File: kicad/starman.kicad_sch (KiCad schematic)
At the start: 204 parts, among them J10 Barrel_Jack_MountingPin, J5 Conn_02x03_Counter_Clockwise, J7 Conn_01x10, J9 Conn_01x10, SW1 SW_SPST, SW2 SW_SPST, U1 ESP32-S2-MINI-1, U2 PCA9959, U3 PCA9959, U4 PCA9959, U5 PCA9959, U6 PCA9959, U7 PCA9959, U8 NCP59301, U9 LF33, Y1 20Mhz, Y2 20Mhz, Y3 20Mhz, Y4 20Mhz, Y5 20Mhz, Y6 20Mhz

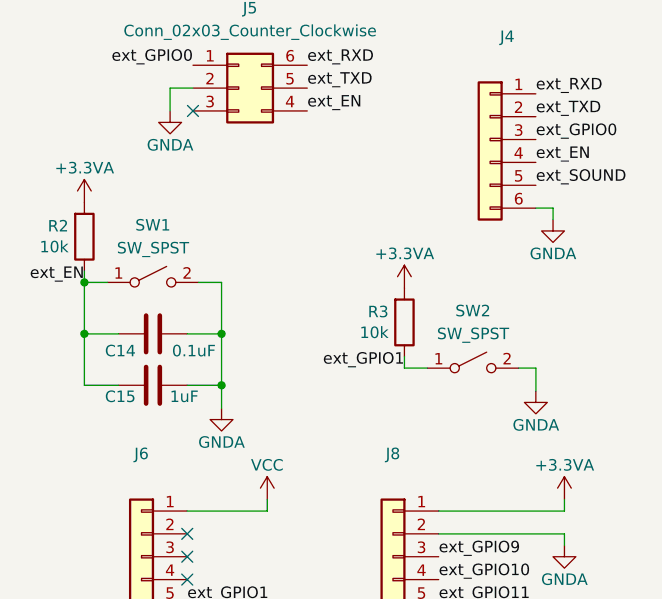
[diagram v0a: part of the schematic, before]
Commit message: Add on headers for an external "Play" button
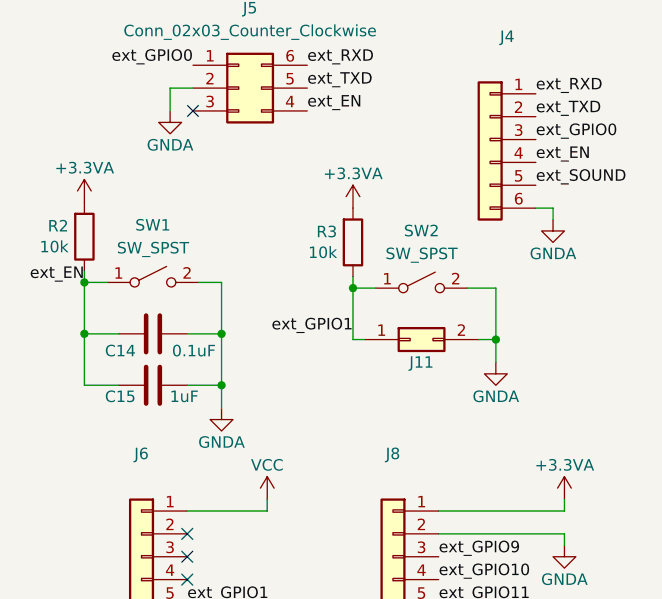
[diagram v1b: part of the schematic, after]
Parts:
- added J11: (no value), symbol Connector_Generic:Conn_02x01
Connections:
- net GNDA: now also J11.2 (Pin_2)
- net ext_GPIO1: now also J11.1 (Pin_1)
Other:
- moved on the sheet: R3, SW2
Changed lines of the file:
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@@
   (junction (at 210.82 88.9) (diameter 0) (color 0 0 0 0)
   )
+  (junction (at 398.145 55.88) (diameter 0) (color 0 0 0 0)
+  )
   (junction (at 144.78 143.51) (diameter 0) (color 0 0 0 0)
   )
@@
   (junction (at 78.74 153.67) (diameter 0) (color 0 0 0 0)
   )
+  (junction (at 382.27 50.165) (diameter 0) (color 0 0 0 0)
+  )
   (junction (at 144.78 45.72) (diameter 0) (color 0 0 0 0)
   )
@@
     (stroke (width 0) (type default) (color 0 0 0 0))
   )
+  (wire (pts (xy 398.145 55.88) (xy 398.145 50.165))
+    (stroke (width 0) (type default) (color 0 0 0 0))
+  )
   (wire (pts (xy 243.84 92.71) (xy 243.84 95.25))
     (stroke (width 0) (type default) (color 0 0 0 0))
@@
     (stroke (width 0) (type default) (color 0 0 0 0))
   )
-  (wire (pts (xy 400.685 59.055) (xy 402.59 59.055))
+  (wire (pts (xy 396.24 55.88) (xy 398.145 55.88))
     (stroke (width 0) (type default) (color 0 0 0 0))
   )
@@
     (stroke (width 0) (type default) (color 0 0 0 0))
   )
+  (wire (pts (xy 382.27 55.88) (xy 383.54 55.88))
+    (stroke (width 0) (type default) (color 0 0 0 0))
+  )
   (wire (pts (xy 144.78 81.28) (xy 142.24 81.28))
     (stroke (width 0) (type default) (color 0 0 0 0))
@@
     (stroke (width 0) (type default) (color 0 0 0 0))
   )
-  (wire (pts (xy 387.985 59.055) (xy 390.525 59.055))
+  (wire (pts (xy 382.27 50.165) (xy 384.81 50.165))
     (stroke (width 0) (type default) (color 0 0 0 0))
   )
@@
     (stroke (width 0) (type default) (color 0 0 0 0))
   )
+  (wire (pts (xy 382.27 50.165) (xy 382.27 55.88))
+    (stroke (width 0) (type default) (color 0 0 0 0))
+  )
   (wire (pts (xy 154.94 115.57) (xy 154.94 114.3))
     (stroke (width 0) (type default) (color 0 0 0 0))
@@
     (stroke (width 0) (type default) (color 0 0 0 0))
   )
+  (wire (pts (xy 398.145 50.165) (xy 394.97 50.165))
+    (stroke (width 0) (type default) (color 0 0 0 0))
+  )
   (wire (pts (xy 144.78 50.8) (xy 142.24 50.8))
     (stroke (width 0) (type default) (color 0 0 0 0))
@@
     (stroke (width 0) (type default) (color 0 0 0 0))
   )
-  (wire (pts (xy 387.985 57.785) (xy 387.985 59.055))
+  (wire (pts (xy 382.27 48.895) (xy 382.27 50.165))
     (stroke (width 0) (type default) (color 0 0 0 0))
   )
@@
     (stroke (width 0) (type default) (color 0 0 0 0))
   )
-  (wire (pts (xy 402.59 59.055) (xy 402.59 61.595))
+  (wire (pts (xy 398.145 55.88) (xy 398.145 58.42))
     (stroke (width 0) (type default) (color 0 0 0 0))
   )
@@
     (effects (font (size 1.27 1.27)) (justify right bottom))
   )
-  (label "ext_GPIO1" (at 387.985 59.055 180)
+  (label "ext_GPIO1" (at 382.27 55.245 180)
     (effects (font (size 1.27 1.27)) (justify right bottom))
   )
@@
     (pin "1")
   )
-  (symbol (lib_id "Device:R") (at 387.985 53.975 0) (mirror x) (unit 1)
+  (symbol (lib_id "Device:R") (at 382.27 45.085 0) (mirror x) (unit 1)
     (in_bom yes) (on_board yes)
-    (property "Reference" "R3" (id 0) (at 386.2324 52.8066 0)
+    (property "Reference" "R3" (id 0) (at 380.5174 43.9166 0)
       (effects (font (size 1.27 1.27)) (justify right))
     )
-    (property "Value" "10k" (id 1) (at 386.2324 55.118 0)
+    (property "Value" "10k" (id 1) (at 380.5174 46.228 0)
       (effects (font (size 1.27 1.27)) (justify right))
     )
-    (property "Footprint" "Resistor_SMD:R_0805_2012Metric" (id 2) (at 386.207 53.975 90)
+    (property "Footprint" "Resistor_SMD:R_0805_2012Metric" (id 2) (at 380.492 45.085 90)
       (effects (font (size 1.27 1.27)) hide)
     )
-    (property "Datasheet" "~" (id 3) (at 387.985 53.975 0)
+    (property "Datasheet" "~" (id 3) (at 382.27 45.085 0)
       (effects (font (size 1.27 1.27)) hide)
     )
@@
     (pin "1")
   )
-  (symbol (lib_id "power:GNDA") (at 402.59 61.595 0) (unit 1)
+  (symbol (lib_id "power:GNDA") (at 398.145 58.42 0) (unit 1)
     (in_bom yes) (on_board yes)
-    (property "Reference" "#PWR031" (id 0) (at 402.59 67.945 0)
+    (property "Reference" "#PWR031" (id 0) (at 398.145 64.77 0)
       (effects (font (size 1.27 1.27)) hide)
     )
-    (property "Value" "GNDA" (id 1) (at 402.59 65.405 0))
-    (property "Footprint" "" (id 2) (at 402.59 61.595 0)
+    (property "Value" "GNDA" (id 1) (at 398.145 62.23 0))
+    (property "Footprint" "" (id 2) (at 398.145 58.42 0)
       (effects (font (size 1.27 1.27)) hide)
     )
-    (property "Datasheet" "" (id 3) (at 402.59 61.595 0)
+    (property "Datasheet" "" (id 3) (at 398.145 58.42 0)
       (effects (font (size 1.27 1.27)) hide)
     )
     (pin "1")
   )
-  (symbol (lib_id "power:+3.3VA") (at 387.985 50.165 0) (unit 1)
+  (symbol (lib_id "Connector_Generic:Conn_02x01") (at 388.62 55.88 0) (unit 1)
     (in_bom yes) (on_board yes)
-    (property "Reference" "#PWR030" (id 0) (at 387.985 53.975 0)
+    (property "Reference" "J11" (id 0) (at 389.89 58.42 0))
+    (property "Value" "" (id 1) (at 389.89 60.96 0))
+    (property "Footprint" "" (id 2) (at 388.62 55.88 0)
       (effects (font (size 1.27 1.27)) hide)
     )
-    (property "Value" "+3.3VA" (id 1) (at 387.985 46.355 0))
-    (property "Footprint" "" (id 2) (at 387.985 50.165 0)
+    (property "Datasheet" "~" (id 3) (at 388.62 55.88 0)
       (effects (font (size 1.27 1.27)) hide)
     )
-    (property "Datasheet" "" (id 3) (at 387.985 50.165 0)
+    (pin "1")
+    (pin "2")
+  )
+  (symbol (lib_id "power:+3.3VA") (at 382.27 41.275 0) (unit 1)
+    (in_bom yes) (on_board yes)
+    (property "Reference" "#PWR030" (id 0) (at 382.27 45.085 0)
+      (effects (font (size 1.27 1.27)) hide)
+    )
+    (property "Value" "+3.3VA" (id 1) (at 382.27 37.465 0))
+    (property "Footprint" "" (id 2) (at 382.27 41.275 0)
+      (effects (font (size 1.27 1.27)) hide)
+    )
+    (property "Datasheet" "" (id 3) (at 382.27 41.275 0)
       (effects (font (size 1.27 1.27)) hide)
     )
@@
     (pin "1")
   )
-  (symbol (lib_id "Switch:SW_SPST") (at 395.605 59.055 0) (unit 1)
+  (symbol (lib_id "Switch:SW_SPST") (at 389.89 50.165 0) (unit 1)
     (in_bom yes) (on_board yes)
-    (property "Reference" "SW2" (id 0) (at 395.605 52.705 0))
-    (property "Value" "SW_SPST" (id 1) (at 395.605 55.245 0))
-    (property "Footprint" "Button_Switch_SMD:SW_SPST_PTS810" (id 2) (at 395.605 59.055 0)
+    (property "Reference" "SW2" (id 0) (at 389.89 43.815 0))
+    (property "Value" "SW_SPST" (id 1) (at 389.89 46.355 0))
+    (property "Footprint" "Button_Switch_SMD:SW_SPST_PTS810" (id 2) (at 389.89 50.165 0)
       (effects (font (size 1.27 1.27)) hide)
     )
-    (property "Datasheet" "~" (id 3) (at 395.605 59.055 0)
+    (property "Datasheet" "~" (id 3) (at 389.89 50.165 0)
       (effects (font (size 1.27 1.27)) hide)
     )
@@
       (reference "J10") (unit 1) (value "Barrel_Jack_MountingPin") (footprint "Connector_BarrelJack:BarrelJack_CUI_PJ-063AH_Horizontal")
     )
+    (path "/56bd17ef-9eb8-4409-8c35-c6c9960995e7"
+      (reference "J11") (unit 1) (value "Conn_02x01") (footprint "Connector_PinHeader_2.54mm:PinHeader_1x02_P2.54mm_Vertical")
+    )
     (path "/515a2d72-1a9d-4aa4-9d0c-cba89acc2e38"

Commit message: Fixed the solderpad for U2..U7 according to match datasheet
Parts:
- J1, J3: value (none) -> M20-8771246; footprint (none) -> Connector_PinHeader_2.54mm:PinHeader_1x12_P2.54mm_Vertical_SMD_Pin1Right
- J11: value (none) -> Conn_02x01; footprint (none) -> Connector_PinHeader_2.54mm:PinHeader_1x02_P2.54mm_Vertical
- J2: value (none) -> M20-8771246; footprint (none) -> Connector_PinHeader_2.54mm:PinHeader_1x06_P2.54mm_Vertical_SMD_Pin1Right
- J4: value (none) -> ESW-106-44-T-S; footprint (none) -> Connector_PinSocket_2.54mm:PinSocket_1x06_P2.54mm_Vertical
- J6, J8: value (none) -> ESW-112-44-T-S; footprint (none) -> Connector_PinSocket_2.54mm:PinSocket_1x12_P2.54mm_Vertical
- TP1: value (none) -> TestPoint; footprint (none) -> TestPoint:TestPoint_Pad_1.5x1.5mm
- U6: value PCA9959 -> (none)
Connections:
- net GND: no longer U2.41 (PAD), U3.41 (PAD), U4.41 (PAD), U5.41 (PAD), U6.41 (PAD), U7.41 (PAD)

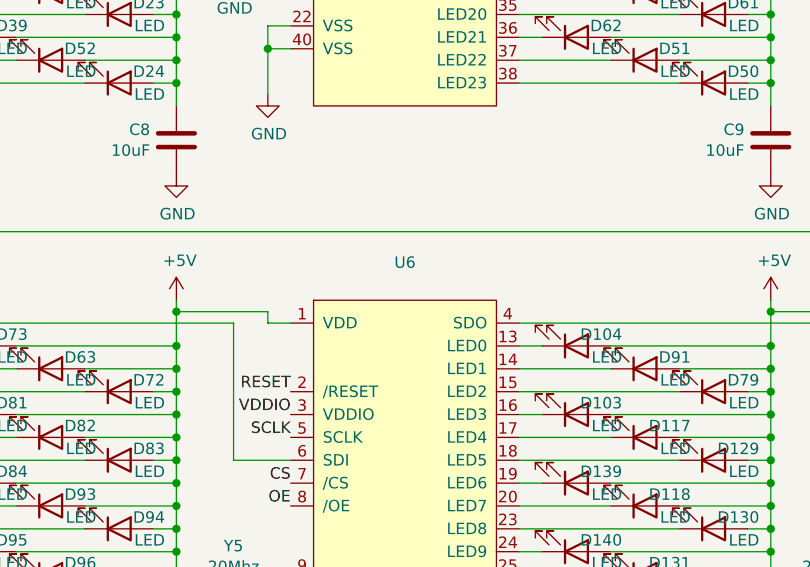
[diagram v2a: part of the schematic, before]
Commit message: Reduce footprint and margins of OSRAM P47F LED
Will be required to allow for space for the NXP chip replacement
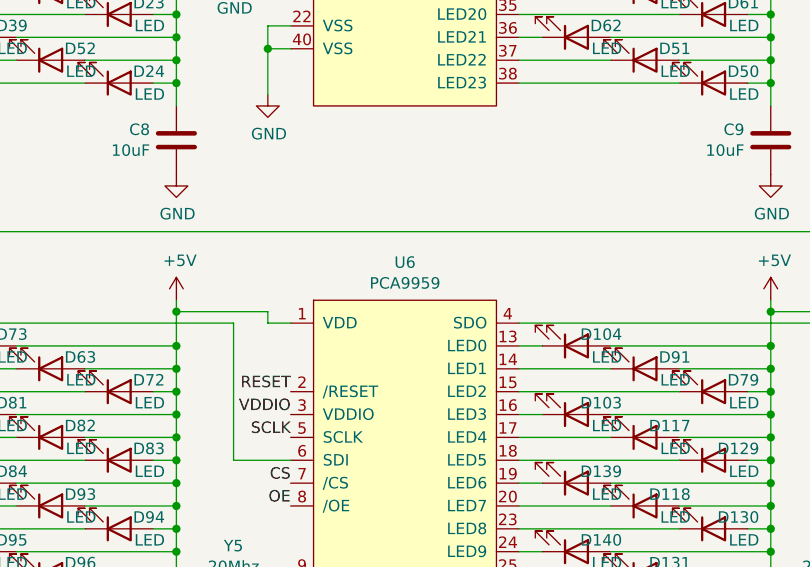
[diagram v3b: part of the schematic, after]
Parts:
- D1, D10, D100, D101, D102, D103, D104, D105, D106, D107, D108, D109, D11, D110, D111, D112, D113, D114, D115, D116, D117, D118, D119, D12, D120, D121, D122, D123, D124, D125, D126, D127, D128, D129, D13, D130, D131, D132, D133, D134, D135, D136, D137, D138, D139, D14, D140, D141, D142, D143, D144, D15, D16, D17, D18, D19, D2, D20, D21, D22, D23, D24, D25, D26, D27, D28, D29, D3, D30, D31, D32, D33, D34, D35, D36, D37, D38, D39, D4, D40, D41, D42, D43, D44, D45, D46, D47, D48, D49, D5, D50, D51, D52, D53, D54, D55, D56, D57, D58, D59, D6, D60, D61, D62, D63, D64, D65, D66, D67, D68, D69, D7, D70, D71, D72, D73, D74, D75, D76, D77, D78, D79, D8, D80, D81, D82, D83, D84, D85, D86, D87, D88, D89, D9, D90, D91, D92, D93, D94, D95, D96, D97, D98, D99: footprint LED_SMD:LED_Osram_Lx_P47F_D2mm_ReverseMount -> starman:LED_Osram_Lx_P47F_D2mm_ReverseMount
- U6: value (none) -> PCA9959

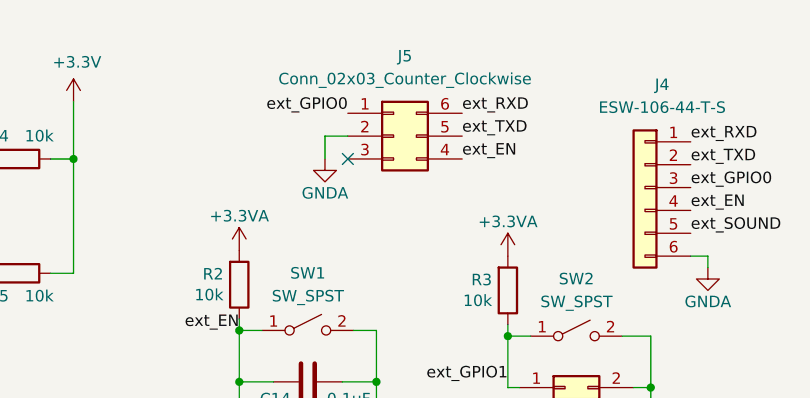
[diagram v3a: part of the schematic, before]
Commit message: Fixed the orientation of J5, moved GND plane to top copper
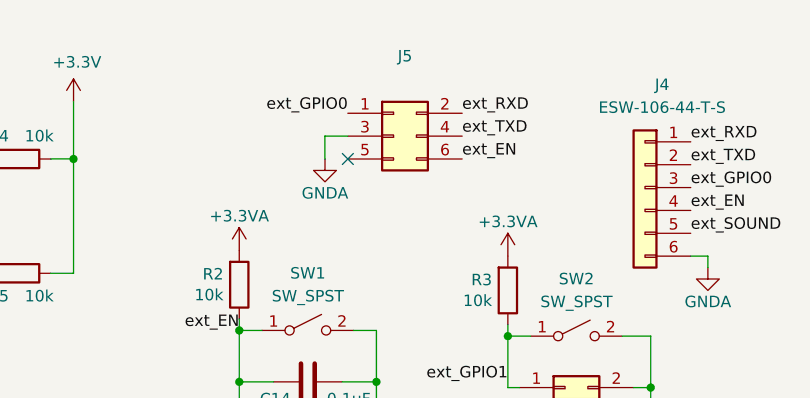
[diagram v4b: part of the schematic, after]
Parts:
- J5: value Conn_02x03_Counter_Clockwise -> (none); footprint Connector_PinHeader_2.54mm:PinHeader_2x03_P2.54mm_Vertical -> (none); symbol Connector_Generic:Conn_02x03_Counter_Clockwise -> Connector_Generic:Conn_02x03_Odd_Even
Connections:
- net GNDA: now also J5.3 (Pin_3); no longer J5.2 (Pin_2)
- net ext_EN: now also J5.6 (Pin_6); no longer J5.4 (Pin_4)
- net ext_RXD: now also J5.2 (Pin_2); no longer J5.6 (Pin_6)
- net ext_TXD: now also J5.4 (Pin_4); no longer J5.5 (Pin_5)
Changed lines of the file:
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@@
     (pin "1")
   )
-  (symbol (lib_id "Connector_Generic:Conn_02x03_Counter_Clockwise") (at 369.57 27.94 0) (unit 1)
+  (symbol (lib_id "Connector_Generic:Conn_02x03_Odd_Even") (at 369.57 27.94 0) (unit 1)
     (in_bom yes) (on_board yes) (fields_autoplaced)
     (property "Reference" "J5" (id 0) (at 370.84 19.05 0))
-    (property "Value" "Conn_02x03_Counter_Clockwise" (id 1) (at 370.84 21.59 0))
-    (property "Footprint" "Connector_PinHeader_2.54mm:PinHeader_2x03_P2.54mm_Vertical" (id 2) (at 369.57 27.94 0)
+    (property "Value" "" (id 1) (at 370.84 21.59 0))
+    (property "Footprint" "" (id 2) (at 369.57 27.94 0)
       (effects (font (size 1.27 1.27)) hide)
     )
@@
     )
     (path "/34d8e8c9-d781-4979-9bfb-50e6442ac62f"
-      (reference "J5") (unit 1) (value "Conn_02x03_Counter_Clockwise") (footprint "Connector_PinHeader_2.54mm:PinHeader_2x03_P2.54mm_Vertical")
+      (reference "J5") (unit 1) (value "Conn_02x03") (footprint "Connector_PinHeader_2.54mm:PinHeader_2x03_P2.54mm_Vertical")
     )
     (path "/42aa9475-b02f-438a-8656-56b92f849b04"

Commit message: Completely replace NXP with LED1642GWTTR
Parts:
- removed U2, U3, U4, U5, U6, U7: PCA9959, starman:QFN-40_EP_5x5_Pitch0.4mm, symbol starman:PCA9959
- removed Y1, Y2, Y3, Y4, Y5, Y6: 20Mhz, Crystal:Resonator_SMD_muRata_CSTxExxV-3Pin_3.0x1.1mm, symbol Device:Crystal_GND2_Small
- added C16, C17, C18: 1uF, Capacitor_SMD:C_0805_2012Metric, symbol Device:C
- added C20, C21, C22, C23, C24, C25, C26, C27, C28, C29, C30, C8: (no value), Capacitor_SMD:C_0805_2012Metric, symbol Device:C
- added R16, R17, R18, R19: (no value), Resistor_SMD:R_0805_2012Metric, symbol Device:R
- added R20: 500k, Resistor_SMD:R_0805_2012Metric, symbol Device:R
- added U10, U3, U4, U5, U6, U7, U8, U9: LED1642GWTTR, Package_SO:TSSOP-24_4.4x7.8mm_P0.65mm, symbol Driver_LED:LED1642GWTTR
- added U2: (no value), symbol Driver_LED:LED1642GWTTR
- added X1: (no value), symbol Oscillator:ECS-2520MV-xxx-xx
- added X2, X3: ECS-2333-300, Oscillator:Oscillator_SMD_ECS_2520MV-xxx-xx-4Pin_2.5x2.0mm, symbol Oscillator:ECS-2520MV-xxx-xx
- C10, C11, C12, C13, C9: value 10uF -> 1uF
- C19: renamed from C8; value 10uF -> (none)
- R10, R11, R12, R13, R8, R9: value 3k -> (none)
- R14: value 10k -> 500k
- R15: value 10k -> (none)
- renumbered U8 to U11, U9 to U12
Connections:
- net +3V3: now also C10.1, C11.1, C12.1, C13.1, C9.1, C16.1, C17.1, C18.1, C8.1, R19.1, R20.1, U10.24 (VDD), U2.24 (VDD), U3.24 (VDD), U4.24 (VDD), U5.24 (VDD), U6.24 (VDD), U7.24 (VDD), U8.24 (VDD), U9.24 (VDD), X3.4 (VDD); no longer R15.1
- net +5V: now also C20.2, C21.2, C22.2, C23.2, C24.2, C25.2, C26.2, C27.2; no longer C10.2, C11.2, C12.2, C13.2, C9.2
- net GND: now also C10.2, C11.2, C12.2, C13.2, C9.2, R15.1, C16.2, C17.2, C18.2, C20.1, C21.1, C22.1, C23.1, C24.1, C25.1, C26.1, C27.1, C28.1, C29.1, C30.1, C8.2, R16.1, R17.1, R18.1, U10.1 (GND), U2.1 (GND), U3.1 (GND), U4.1 (GND), U5.1 (GND), U6.1 (GND), U7.1 (GND), U8.1 (GND), U9.1 (GND), X1.2 (GND), X2.2 (GND), X3.2 (GND); no longer C10.1, C11.1, C12.1, C13.1, C9.1
- net MISO: now also U10.22 (SDO)
- net MOSI: now also U2.2 (SDI)
- net SCLK: now also U10.3 (CLK), U2.3 (CLK), U3.3 (CLK), U4.3 (CLK), U5.3 (CLK), U6.3 (CLK), U7.3 (CLK), U8.3 (CLK), U9.3 (CLK)
- net at D85.1 (K): now also U7.10 (OUT5)
- net at D86.1 (K): now also U7.11 (OUT6)
- net at D87.1 (K): now also U7.12 (OUT7)
- net at D88.1 (K): now also U7.13 (OUT8)
- net at D89.1 (K): now also U7.17 (OUT12)
- net at D1.1 (K): now also U2.6 (OUT1)
- net at D2.1 (K): now also U2.19 (OUT14)
- net at D3.1 (K): now also U2.7 (OUT2)
- net at D4.1 (K): now also U2.5 (OUT0)
- net at D5.1 (K): now also U2.20 (OUT15)
- net at D6.1 (K): now also U2.18 (OUT13)
- net at D7.1 (K): now also U2.8 (OUT3)
- net at D8.1 (K): now also U2.12 (OUT7)
- net at D9.1 (K): now also U2.13 (OUT8)
- net at D10.1 (K): now also U2.17 (OUT12)
- net at D11.1 (K): now also U2.9 (OUT4)
- net at D12.1 (K): now also U2.10 (OUT5)
- net at D13.1 (K): now also U2.11 (OUT6)
- net at D14.1 (K): now also U2.14 (OUT9)
- net at D15.1 (K): now also U2.15 (OUT10)
- net at D16.1 (K): now also U2.16 (OUT11)
- net at D17.1 (K): now also U3.13 (OUT8)
- net at D18.1 (K): now also U3.14 (OUT9)
- net at D19.1 (K): now also U3.10 (OUT5)
- net at D20.1 (K): now also U3.11 (OUT6)
- net at D21.1 (K): now also U3.12 (OUT7)
- net at D22.1 (K): now also U4.15 (OUT10)
- net at D23.1 (K): now also U4.14 (OUT9)
- net at D24.1 (K): now also U4.13 (OUT8)
- net at D25.1 (K): now also U4.12 (OUT7)
- net at D26.1 (K): now also U4.11 (OUT6)
- net at D27.1 (K): now also U4.10 (OUT5)
- net at D28.1 (K): now also U5.13 (OUT8)
- net at D29.1 (K): now also U5.14 (OUT9)
- net at D30.1 (K): now also U5.15 (OUT10)
- net at D31.1 (K): now also U5.11 (OUT6)
- net at D32.1 (K): now also U5.12 (OUT7)
- net at D33.1 (K): now also U3.17 (OUT12)
- net at D34.1 (K): now also U3.16 (OUT11)
- net at D35.1 (K): now also U3.15 (OUT10)
- net at D36.1 (K): now also U3.9 (OUT4)
- net at D37.1 (K): now also U3.8 (OUT3)
- net at D38.1 (K): now also U4.17 (OUT12)
- net at D39.1 (K): now also U4.20 (OUT15)
- net at D40.1 (K): now also U4.5 (OUT0)
- net at D41.1 (K): now also U4.9 (OUT4)
- net at D42.1 (K): now also U5.17 (OUT12)
- net at D43.1 (K): now also U5.16 (OUT11)
- net at D44.1 (K): now also U5.10 (OUT5)
- net at D45.1 (K): now also U5.9 (OUT4)
- net at D46.1 (K): now also U5.8 (OUT3)
- net at D47.1 (K): now also U3.18 (OUT13)
- net at D48.1 (K): now also U3.20 (OUT15)
- net at D49.1 (K): now also U3.5 (OUT0)
- net at D50.1 (K): now also U3.7 (OUT2)
- net at D51.1 (K): now also U4.16 (OUT11)
- net at D52.1 (K): now also U4.19 (OUT14)
- net at D53.1 (K): now also U4.6 (OUT1)
- net at D54.1 (K): now also U4.8 (OUT3)
- net at D55.1 (K): now also U5.18 (OUT13)
- net at D56.1 (K): now also U5.20 (OUT15)
- net at D57.1 (K): now also U5.5 (OUT0)
- net at D58.1 (K): now also U5.7 (OUT2)
- net at D59.1 (K): now also U3.19 (OUT14)
- net at D60.1 (K): now also U3.6 (OUT1)
- net at D61.1 (K): now also U6.19 (OUT14)
- net at D62.1 (K): now also U6.20 (OUT15)
- net at D63.1 (K): now also U4.18 (OUT13)
- net at D64.1 (K): now also U4.7 (OUT2)
- net at D65.1 (K): now also U7.5 (OUT0)
- net at D66.1 (K): now also U7.6 (OUT1)
- net at D67.1 (K): now also U5.19 (OUT14)
- net at D68.1 (K): now also U5.6 (OUT1)
- net at D69.1 (K): now also U6.6 (OUT1)
- net at D70.1 (K): now also U6.5 (OUT0)
- net at D71.1 (K): now also U6.18 (OUT13)
- net at D72.1 (K): now also U6.17 (OUT12)
- net at D73.1 (K): now also U6.16 (OUT11)
- net at D74.1 (K): now also U7.9 (OUT4)
- net at D75.1 (K): now also U7.8 (OUT3)
- net at D76.1 (K): now also U7.7 (OUT2)
- net at D77.1 (K): now also U7.20 (OUT15)
- net at D78.1 (K): now also U7.19 (OUT14)
- net at D79.1 (K): now also U6.7 (OUT2)
- net at D80.1 (K): now also U6.8 (OUT3)
- net at D81.1 (K): now also U6.12 (OUT7)
- net at D82.1 (K): now also U6.13 (OUT8)
- net at D83.1 (K): now also U6.14 (OUT9)
- net at D84.1 (K): now also U6.15 (OUT10)
- net at D141.1 (K): now also U8.7 (OUT2)
- net at D140.1 (K): now also U8.8 (OUT3)
- net at D139.1 (K): now also U8.9 (OUT4)
- net at D144.1 (K): now also U10.16 (OUT11)
- net at D143.1 (K): now also U10.17 (OUT12)
- net at D142.1 (K): now also U10.18 (OUT13)
- net at D133.1 (K): now also U8.14 (OUT9)
- net at D134.1 (K): now also U10.11 (OUT6)
- net at D135.1 (K): now also U10.12 (OUT7)
- net at D136.1 (K): now also U10.13 (OUT8)
- net at D137.1 (K): now also U10.14 (OUT9)
- net at D121.1 (K): now also U9.10 (OUT5)
- net at D122.1 (K): now also U9.11 (OUT6)
- net at D123.1 (K): now also U9.14 (OUT9)
- net at D124.1 (K): now also U9.15 (OUT10)
- net at D125.1 (K): now also U10.10 (OUT5)
- net at D126.1 (K): now also U10.5 (OUT0)
- net at D127.1 (K): now also U10.20 (OUT15)
- net at D128.1 (K): now also U10.19 (OUT14)
- net at D129.1 (K): now also U8.10 (OUT5)
- net at D130.1 (K): now also U8.11 (OUT6)
- net at D131.1 (K): now also U8.12 (OUT7)
- net at D132.1 (K): now also U8.13 (OUT8)
- net at D138.1 (K): now also U10.15 (OUT10)
- net at D109.1 (K): now also U9.12 (OUT7)
- net at D110.1 (K): now also U9.13 (OUT8)
- net at D111.1 (K): now also U9.17 (OUT12)
- net at D112.1 (K): now also U9.16 (OUT11)
- net at D113.1 (K): now also U10.6 (OUT1)
- net at D97.1 (K): now also U9.20 (OUT15)
- net at D98.1 (K): now also U9.19 (OUT14)
- net at D99.1 (K): now also U9.18 (OUT13)
- net at D100.1 (K): now also U7.16 (OUT11)
- net at D101.1 (K): now also U7.15 (OUT10)
- net at D102.1 (K): now also U7.14 (OUT9)
- net at D103.1 (K): now also U8.16 (OUT11)
- net at D104.1 (K): now also U8.17 (OUT12)
- net at D105.1 (K): now also U8.18 (OUT13)
- net at D106.1 (K): now also U8.19 (OUT14)
- net at D107.1 (K): now also U9.9 (OUT4)
- net at D108.1 (K): now also U9.8 (OUT3)
- net at D118.1 (K): now also U8.5 (OUT0)
- net at D119.1 (K): now also U8.20 (OUT15)
- net at D120.1 (K): now also U8.15 (OUT10)
- net at D114.1 (K): now also U10.7 (OUT2)
- net at D115.1 (K): now also U10.8 (OUT3)
- net at D116.1 (K): now also U10.9 (OUT4)
- net at D117.1 (K): now also U8.6 (OUT1)
- net at D93.1 (K): now also U6.9 (OUT4)
- net at D92.1 (K): now also U6.10 (OUT5)
- net at D91.1 (K): now also U6.11 (OUT6)
- net at D90.1 (K): now also U7.18 (OUT13)
- net at D96.1 (K): now also U9.5 (OUT0)
- net at D95.1 (K): now also U9.6 (OUT1)
- net at D94.1 (K): now also U9.7 (OUT2)
- net at R8.2: now also U2.23 (R-EXT)
- net at R9.2: now also U3.23 (R-EXT)
- net at R10.2: now also U4.23 (R-EXT)
- net at R11.2: now also U5.23 (R-EXT)
- net at R12.2: now also U6.23 (R-EXT)
- net at R13.2: now also U7.23 (R-EXT)
- net CS: no longer names the net of U1.33 (GPIO37)
- net OE: no longer names the net of U1.34 (GPIO38)
- net OE: no longer R14.2
- net RESET renamed LE
- net LE: now also U10.4 (LE), U2.4 (LE), U3.4 (LE), U4.4 (LE), U5.4 (LE), U6.4 (LE), U7.4 (LE), U8.4 (LE), U9.4 (LE)
- new net: U7.22 (SDO), U8.2 (SDI)
- new net: U8.22 (SDO), U9.2 (SDI)
- new net: R16.2, U8.23 (R-EXT)
- new net: U10.2 (SDI), U9.22 (SDO)
- new net: R17.2, U9.23 (R-EXT)
- new net: U6.22 (SDO), U7.2 (SDI)
- new net: U3.22 (SDO), U4.2 (SDI)
- new net: U4.22 (SDO), U5.2 (SDI)
- new net: U2.22 (SDO), U3.2 (SDI)
- new net: R18.2, U10.23 (R-EXT)
- new net: U5.22 (SDO), U6.2 (SDI)
- new net PWCLK1: C28.2, U2.21 (PWCLK), U3.21 (PWCLK), U4.21 (PWCLK), X1.3 (OUT)
- new net PWCLK2: C29.2, U6.21 (PWCLK), U8.21 (PWCLK), U9.21 (PWCLK), X2.3 (OUT)
- new net PWCLK3: C30.2, R19.2, U10.21 (PWCLK), U5.21 (PWCLK), U7.21 (PWCLK), X3.3 (OUT)
- no-connect marks 16 -> 20
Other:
- moved on the sheet: C19, C4, C5, C6, C7, D1, D10, D100, D101, D102, D103, D104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
